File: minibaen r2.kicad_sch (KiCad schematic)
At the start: 134 parts, among them SW1 SW_Push, SW2 RotaryEncoder_Switch, U1 ATmega32U2-A, U2 PRTR5V0U2X, Y1 Crystal_GND24_Small

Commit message: stagger
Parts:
- removed C1: 4.7n, Capacitor_SMD:C_0603_1608Metric, symbol Device:C_Small
- removed C2, C4: 22pF, Capacitor_SMD:C_0603_1608Metric, symbol Device:C_Small
- removed C3: 1uF, Capacitor_SMD:C_0603_1608Metric, symbol Device:C_Small
- removed C5, C6: 0.1uF, Capacitor_SMD:C_0603_1608Metric, symbol Device:C_Small
- removed C7: 10uF, Capacitor_SMD:C_0603_1608Metric, symbol Device:C_Small
- removed D46, D47, D48, D49, D50, D51, D52: D_Small, Diode_SMD:D_SOD-123, symbol Device:D_Small
- removed F1: 500mA, Fuse:Fuse_1206_3216Metric, symbol Device:Polyfuse_Small
- removed MX1, MX10, MX11, MX12, MX13, MX14, MX15, MX16, MX17, MX18, MX19, MX2, MX20, MX21, MX22, MX23, MX24, MX25, MX26, MX27, MX28, MX29, MX3, MX30, MX31, MX32, MX33, MX34, MX35, MX36, MX37, MX38, MX39, MX4, MX40, MX41, MX42, MX43, MX44, MX45, MX46, MX47, MX48, MX49, MX5, MX50, MX51, MX52, MX6, MX7, MX8, MX9: MX-NoLED, MX_Only:MXOnly-1U-NoLED, symbol keybage:MX-NoLED
- removed MX53, MX57: MX-NoLED, MX_Only:MXOnly-2U-ReversedStabilizers-NoLED, symbol keybage:MX-NoLED
- removed MX54, MX56, MX58: MX-NoLED, MX_Only:MXOnly-3U-ReversedStabilizers-NoLED, symbol keybage:MX-NoLED
- removed MX55: MX-NoLED, MX_Only:MXOnly-7U-ReversedStabilizers-NoLED, symbol keybage:MX-NoLED
- removed R1: 10k, Resistor_SMD:R_0603_1608Metric, symbol Device:R_Small
- removed R2: 22, Resistor_SMD:R_0603_1608Metric, symbol Device:R_Small
- removed R5, R6: 5k1, Resistor_SMD:R_0603_1608Metric, symbol Device:R_Small
- removed R7: 1M, Resistor_SMD:R_0603_1608Metric, symbol Device:R_Small
- removed SW1: SW_Push, Connector_PinHeader_2.54mm:PinHeader_1x02_P2.54mm_Vertical, symbol Switch:SW_Push
- removed SW2: RotaryEncoder_Switch, keebio:RotaryEncoder_EC11-no-legs, symbol Device:RotaryEncoder_Switch
- removed U1: ATmega32U2-A, Package_QFP:TQFP-32_7x7mm_P0.8mm, symbol MCU_Microchip_ATmega:ATmega32U2-A
- removed U2: PRTR5V0U2X, Package_TO_SOT_SMD:SOT-143, symbol keebio:PRTR5V0U2X
- removed USB1: HRO-TYPE-C-31-M-12, Type-C:HRO-TYPE-C-31-M-12, symbol Type-C:HRO-TYPE-C-31-M-12
- removed Y1: Crystal_GND24_Small, Crystal:Crystal_SMD_3225-4Pin_3.2x2.5mm, symbol Device:Crystal_GND24_Small
- added C10, C11, C8, C9: 100nF, Capacitor_SMD:C_0402_1005Metric, symbol Device:C_Small
- added C12: 10nF, Capacitor_SMD:C_0402_1005Metric, symbol Device:C_Small
- added C13, C14, C19: 4.7uF, Capacitor_SMD:C_0402_1005Metric, symbol Device:C_Small
- added C15, C16, C17, C18: 1uF, Capacitor_SMD:C_0402_1005Metric, symbol Device:C_Small
- added F1: 500mA, Fuse:Fuse_0603_1608Metric, symbol Device:Fuse_Small
- added J1: USB_C_Receptacle_USB2.0, Connector_USB:USB_C_Receptacle_HRO_TYPE-C-31-M-12, symbol Connector:USB_C_Receptacle_USB2.0
- added Q1: 2N7002, Package_TO_SOT_SMD:SOT-23, symbol Transistor_FET:2N7002
- added R10, R11: 10k, Resistor_SMD:R_0402_1005Metric, symbol Device:R_Small
- added R12: 100k, Resistor_SMD:R_0402_1005Metric, symbol Device:R_Small
- added S1: MX_stab, marbastlib-mx:STAB_MX_2.75u, symbol marbastlib-mx:MX_stab
- added S2: MX_stab, marbastlib-mx:STAB_MX_3u, symbol marbastlib-mx:MX_stab
- added S3: MX_stab, marbastlib-mx:STAB_MX_2u, symbol marbastlib-mx:MX_stab
- added SW1, SW10, SW11, SW12, SW13, SW15, SW16, SW17, SW18, SW19, SW2, SW20, SW21, SW22, SW23, SW24, SW27, SW28, SW29, SW3, SW30, SW31, SW32, SW33, SW34, SW35, SW36, SW39, SW4, SW41, SW42, SW44, SW5, SW6, SW7, SW8, SW9: MX_SW_solder, marbastlib-mx:SW_MX_1u, symbol marbastlib-mx:MX_SW_solder
- added SW14, SW37, SW38, SW40, SW43, SW45: MX_SW_solder, marbastlib-mx:SW_MX_1.25u, symbol marbastlib-mx:MX_SW_solder
- added SW25, SW26: MX_SW_solder, marbastlib-mx:SW_MX_1.75u, symbol marbastlib-mx:MX_SW_solder
- added SW46: SW_Push, Button_Switch_SMD:SW_SPST_TL3342, symbol Switch:SW_Push
- added U3: SRV05-4, marbastlib-various:SOT-23-6-routable, symbol Power_Protection:SRV05-4
- added U4: XC6206PxxxMR, Package_TO_SOT_SMD:SOT-23, symbol Regulator_Linear:XC6206PxxxMR
- added U5: STM32F072C8Tx, Package_QFP:LQFP-48_7x7mm_P0.5mm, symbol MCU_ST_STM32F0:STM32F072C8Tx
- R3: value 22 -> 5k1; footprint Resistor_SMD:R_0603_1608Metric -> Resistor_SMD:R_0402_1005Metric
- R4: value 10k -> 5k1; footprint Resistor_SMD:R_0603_1608Metric -> Resistor_SMD:R_0402_1005Metric
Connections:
- net DP- is gone; now on net GND: R3.1
- net +5V: now also C16.2, F1.2, U4.3 (VI)
- net D+: now also J1.A6 (D+), J1.B6 (D+), U3.3 (IO2), U5.33 (PA12)
- net D-: now also J1.A7 (D-), J1.B7 (D-), U3.4 (IO3), U5.32 (PA11); no longer R3.2
- net GND: now also C10.2, C11.2, C12.2, C13.2, C14.2, C15.2, C16.1, C17.1, C18.2, C8.2, C9.2, J1.A1 (GND), J1.A12 (GND), J1.B1 (GND), J1.B12 (GND), J1.S1 (SHIELD), Q1.2 (S), R11.2, R12.2, U3.2 (VN), U4.1 (GND), U5.23 (VSS), U5.35 (VSS), U5.47 (VSS), U5.8 (VSSA)
- net col0: now also SW1.1, SW14.1, SW26.1, SW38.1, U5.18 (PB0)
- net col1: now also SW15.1, SW2.1, SW39.1, U5.17 (PA7)
- net col10: now also SW11.1, SW24.1, SW35.1, SW43.1, U5.25 (PB12)
- net col11: now also SW12.2, SW36.1, SW44.1, U5.37 (PA14)
- net col12: now also SW13.1, SW25.1, SW37.1, SW45.1, U5.46 (PB9)
- net col2: now also SW16.1, SW27.1, SW3.1, U5.16 (PA6)
- net col3: now also SW17.1, SW28.1, SW4.1, SW40.1, U5.15 (PA5)
- net col4: now also SW18.1, SW29.1, SW5.1, U5.31 (PA10)
- net col5: now also SW19.1, SW30.1, SW41.1, SW6.1, U5.30 (PA9)
- net col6: now also SW20.1, SW31.1, SW7.1, U5.29 (PA8)
- net col7: now also SW21.1, SW32.1, SW8.1, U5.28 (PB15)
- net col8: now also SW22.1, SW33.1, SW42.1, SW9.1, U5.27 (PB14)
- net col9: now also SW10.1, SW23.1, SW34.1, U5.26 (PB13)
- net row0: now also U5.38 (PA15)
- net row1: now also U5.41 (PB5); no longer D26.1 (K)
- net row2: now also D26.1 (K), U5.40 (PB4); no longer D38.1 (K), D39.1 (K)
- net row3: now also D38.1 (K), D39.1 (K), U5.39 (PB3)
- net at R4.2: now also J1.B5 (CC2)
- net at D43.2 (A): now also SW43.2
- net at D3.2 (A): now also SW3.2
- net at D39.2 (A): now also SW39.2
- net at D8.2 (A): now also SW8.2
- net at D25.2 (A): now also SW25.2
- net at D21.2 (A): now also SW21.2
- net at D2.2 (A): now also SW2.2
- net at D12.2 (A): now also SW12.1
- net at D33.2 (A): now also SW33.2
- net at D28.2 (A): now also SW28.2
- net at D19.2 (A): now also SW19.2
- net at D45.2 (A): now also SW45.2
- net at D38.2 (A): now also SW38.2
- net at D35.2 (A): now also SW35.2
- net at D22.2 (A): now also SW22.2
- net at D11.2 (A): now also SW11.2
- net at D1.2 (A): now also SW1.2
- net at D42.2 (A): now also SW42.2
- net at D13.2 (A): now also SW13.2
- net at D34.2 (A): now also SW34.2
- net at D7.2 (A): now also SW7.2
- net at D23.2 (A): now also SW23.2
- net at D41.2 (A): now also SW41.2
- net at D14.2 (A): now also SW14.2
- net at D40.2 (A): now also SW40.2
- net at D44.2 (A): now also SW44.2
- net at D24.2 (A): now also SW24.2
- net at D4.2 (A): now also SW4.2
- net at D15.2 (A): now also SW15.2
- net at D10.2 (A): now also SW10.2
- net at D9.2 (A): now also SW9.2
- net at D20.2 (A): now also SW20.2
- net at D16.2 (A): now also SW16.2
- net at D36.2 (A): now also SW36.2
- net at D6.2 (A): now also SW6.2
- net at D18.2 (A): now also SW18.2
- net at D31.2 (A): now also SW31.2
- net at D17.2 (A): now also SW17.2
- net at D30.2 (A): now also SW30.2
- net at D27.2 (A): now also SW27.2
- net at D5.2 (A): now also SW5.2
- net at D37.2 (A): now also SW37.2
- net at D32.2 (A): now also SW32.2
- net at D26.2 (A): now also SW26.2
- net at D29.2 (A): now also SW29.2
- new net: C19.2, Q1.1 (G), R12.1
- new net: J1.A5 (CC1), R3.2
- new net +3V3: C10.1, C11.1, C12.1, C13.1, C14.1, C15.1, C17.2, C8.1, C9.1, R10.1, SW46.2, U4.2 (VO), U5.1 (VBAT), U5.24 (VDD), U5.36 (VDDIO2), U5.48 (VDD), U5.9 (VDDA)
- new net BOOT0: C19.1, R11.1, SW46.1, U5.44 (BOOT0)
- new net NRST: C18.1, Q1.3 (D), R10.2, U5.7 (NRST)
- new net VBUS: F1.1, J1.A4 (VBUS), J1.A9 (VBUS), J1.B4 (VBUS), J1.B9 (VBUS), U3.5 (VP)
- no-connect marks 2 -> 4
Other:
- note added: "Decoupling Capacitors"
- note added: "ESD Protection"
- note added: "MCU"
- note added: "Reset Switch"
- note added: "USB"
- note added: "Voltage Regulator"
- moved on the sheet: H1, H2, H3

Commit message: uhhhhh
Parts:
- added H4, H5: MountingHole, MountingHole:MountingHole_2.2mm_M2_DIN965_Pad, symbol Mechanical:MountingHole
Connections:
- net col4: now also U5.14 (PA4); no longer U5.31 (PA10)
- net col5: now also U5.13 (PA3); no longer U5.30 (PA9)
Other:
- moved on the sheet: H1, H2, H3
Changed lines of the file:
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@@
     (stroke (width 0) (type default))
   )
+  (polyline (pts (xy 156.972 57.658) (xy 156.972 11.938))
+    (stroke (width 0) (type default))
+  )
   (wire (pts (xy 52.324 146.05) (xy 52.324 157.48))
     (stroke (width 0) (type default))
@@
     (stroke (width 0) (type default))
   )
+  (polyline (pts (xy 201.422 113.538) (xy 201.422 57.658))
+    (stroke (width 0) (type default))
+  )
   (wire (pts (xy 101.092 18.288) (xy 106.172 18.288))
     (stroke (width 0) (type default))
@@
     )
   )
-  (global_label "col4" (shape input) (at 57.912 80.518 0) (fields_autoplaced)
+  (global_label "col4" (shape input) (at 57.912 65.278 0) (fields_autoplaced)
     (effects (font (size 1.27 1.27)) (justify left))
-    (property "Intersheetrefs" "${INTERSHEET_REFS}" (at 65.0252 80.518 0)
+    (property "Intersheetrefs" "${INTERSHEET_REFS}" (at 65.0252 65.278 0)
       (effects (font (size 1.27 1.27)) (justify left) hide)
     )
@@
     )
   )
-  (global_label "col5" (shape input) (at 57.912 77.978 0) (fields_autoplaced)
+  (global_label "col5" (shape input) (at 57.912 62.738 0) (fields_autoplaced)
     (effects (font (size 1.27 1.27)) (justify left))
-    (property "Intersheetrefs" "${INTERSHEET_REFS}" (at 65.0252 77.978 0)
+    (property "Intersheetrefs" "${INTERSHEET_REFS}" (at 65.0252 62.738 0)
       (effects (font (size 1.27 1.27)) (justify left) hide)
     )
@@
     )
   )
-  (symbol (lib_id "Mechanical:MountingHole") (at 226.187 16.764 0) (unit 1)
+  (symbol (lib_id "Mechanical:MountingHole") (at 70.866 32.512 0) (unit 1)
     (in_bom yes) (on_board yes) (dnp no) (fields_autoplaced)
-    (property "Reference" "H1" (at 229.997 16.1289 0)
+    (property "Reference" "H1" (at 74.676 31.8769 0)
       (effects (font (size 1.27 1.27)) (justify left))
     )
-    (property "Value" "MountingHole" (at 229.997 18.6689 0)
+    (property "Value" "MountingHole" (at 74.676 34.4169 0)
       (effects (font (size 1.27 1.27)) (justify left))
     )
-    (property "Footprint" "MountingHole:MountingHole_2.2mm_M2_DIN965_Pad" (at 226.187 16.764 0)
+    (property "Footprint" "MountingHole:MountingHole_2.2mm_M2_DIN965_Pad" (at 70.866 32.512 0)
       (effects (font (size 1.27 1.27)) hide)
     )
-    (property "Datasheet" "~" (at 226.187 16.764 0)
+    (property "Datasheet" "~" (at 70.866 32.512 0)
       (effects (font (size 1.27 1.27)) hide)
     )
@@
     )
   )
+  (symbol (lib_id "Mechanical:MountingHole") (at 90.424 37.846 0) (unit 1)
+    (in_bom yes) (on_board yes) (dnp no) (fields_autoplaced)
+    (property "Reference" "H5" (at 94.234 37.2109 0)
+      (effects (font (size 1.27 1.27)) (justify left))
+    )
+    (property "Value" "MountingHole" (at 94.234 39.7509 0)
+      (effects (font (size 1.27 1.27)) (justify left))
+    )
+    (property "Footprint" "MountingHole:MountingHole_2.2mm_M2_DIN965_Pad" (at 90.424 37.846 0)
+      (effects (font (size 1.27 1.27)) hide)
+    )
+    (property "Datasheet" "~" (at 90.424 37.846 0)
+      (effects (font (size 1.27 1.27)) hide)
+    )
+    (instances
+      (project "minibaen r2"
+        (path "/f373dbbd-24c9-4966-b78d-facf605ea15a"
+          (reference "H5") (unit 1)
+        )
+      )
+    )
+  )
   (symbol (lib_id "power:GND") (at 41.402 98.298 0) (unit 1)
     (in_bom yes) (on_board yes) (dnp no) (fields_autoplaced)
@@
     )
   )
+  (symbol (lib_id "Mechanical:MountingHole") (at 90.424 32.766 0) (unit 1)
+    (in_bom yes) (on_board yes) (dnp no) (fields_autoplaced)
+    (property "Reference" "H4" (at 94.234 32.1309 0)
+      (effects (font (size 1.27 1.27)) (justify left))
+    )
+    (property "Value" "MountingHole" (at 94.234 34.6709 0)
+      (effects (font (size 1.27 1.27)) (justify left))
+    )
+    (property "Footprint" "MountingHole:MountingHole_2.2mm_M2_DIN965_Pad" (at 90.424 32.766 0)
+      (effects (font (size 1.27 1.27)) hide)
+    )
+    (property "Datasheet" "~" (at 90.424 32.766 0)
+      (effects (font (size 1.27 1.27)) hide)
+    )
+    (instances
+      (project "minibaen r2"
+        (path "/f373dbbd-24c9-4966-b78d-facf605ea15a"
+          (reference "H4") (unit 1)
+        )
+      )
+    )
+  )
   (symbol (lib_id "Device:D_Small") (at 57.404 153.67 90) (unit 1)
     (in_bom yes) (on_board yes) (dnp no)
@@
     )
   )
-  (symbol (lib_id "Mechanical:MountingHole") (at 232.537 16.764 0) (unit 1)
+  (symbol (lib_id "Mechanical:MountingHole") (at 70.866 37.592 0) (unit 1)
     (in_bom yes) (on_board yes) (dnp no) (fields_autoplaced)
-    (property "Reference" "H2" (at 236.347 16.1289 0)
+    (property "Reference" "H2" (at 74.676 36.9569 0)
       (effects (font (size 1.27 1.27)) (justify left))
     )
-    (property "Value" "MountingHole" (at 236.347 18.6689 0)
+    (property "Value" "MountingHole" (at 74.676 39.4969 0)
       (effects (font (size 1.27 1.27)) (justify left))
     )
-    (property "Footprint" "MountingHole:MountingHole_2.2mm_M2_DIN965_Pad" (at 232.537 16.764 0)
+    (property "Footprint" "MountingHole:MountingHole_2.2mm_M2_DIN965_Pad" (at 70.866 37.592 0)
       (effects (font (size 1.27 1.27)) hide)
     )
-    (property "Datasheet" "~" (at 232.537 16.764 0)
+    (property "Datasheet" "~" (at 70.866 37.592 0)
       (effects (font (size 1.27 1.27)) hide)
     )
@@
     )
   )
-  (symbol (lib_id "Mechanical:MountingHole") (at 242.062 16.764 0) (unit 1)
+  (symbol (lib_id "Mechanical:MountingHole") (at 70.866 42.418 0) (unit 1)
     (in_bom yes) (on_board yes) (dnp no) (fields_autoplaced)
-    (property "Reference" "H3" (at 245.237 16.1289 0)
+    (property "Reference" "H3" (at 74.041 41.7829 0)
       (effects (font (size 1.27 1.27)) (justify left))
     )
-    (property "Value" "MountingHole" (at 245.237 18.6689 0)
+    (property "Value" "MountingHole" (at 74.041 44.3229 0)
       (effects (font (size 1.27 1.27)) (justify left))
     )
-    (property "Footprint" "MountingHole:MountingHole_2.2mm_M2_DIN965_Pad" (at 242.062 16.764 0)
+    (property "Footprint" "MountingHole:MountingHole_2.2mm_M2_DIN965_Pad" (at 70.866 42.418 0)
       (effects (font (size 1.27 1.27)) hide)
     )
-    (property "Datasheet" "~" (at 242.062 16.764 0)
+    (property "Datasheet" "~" (at 70.866 42.418 0)
       (effects (font (size 1.27 1.27)) hide)
     )

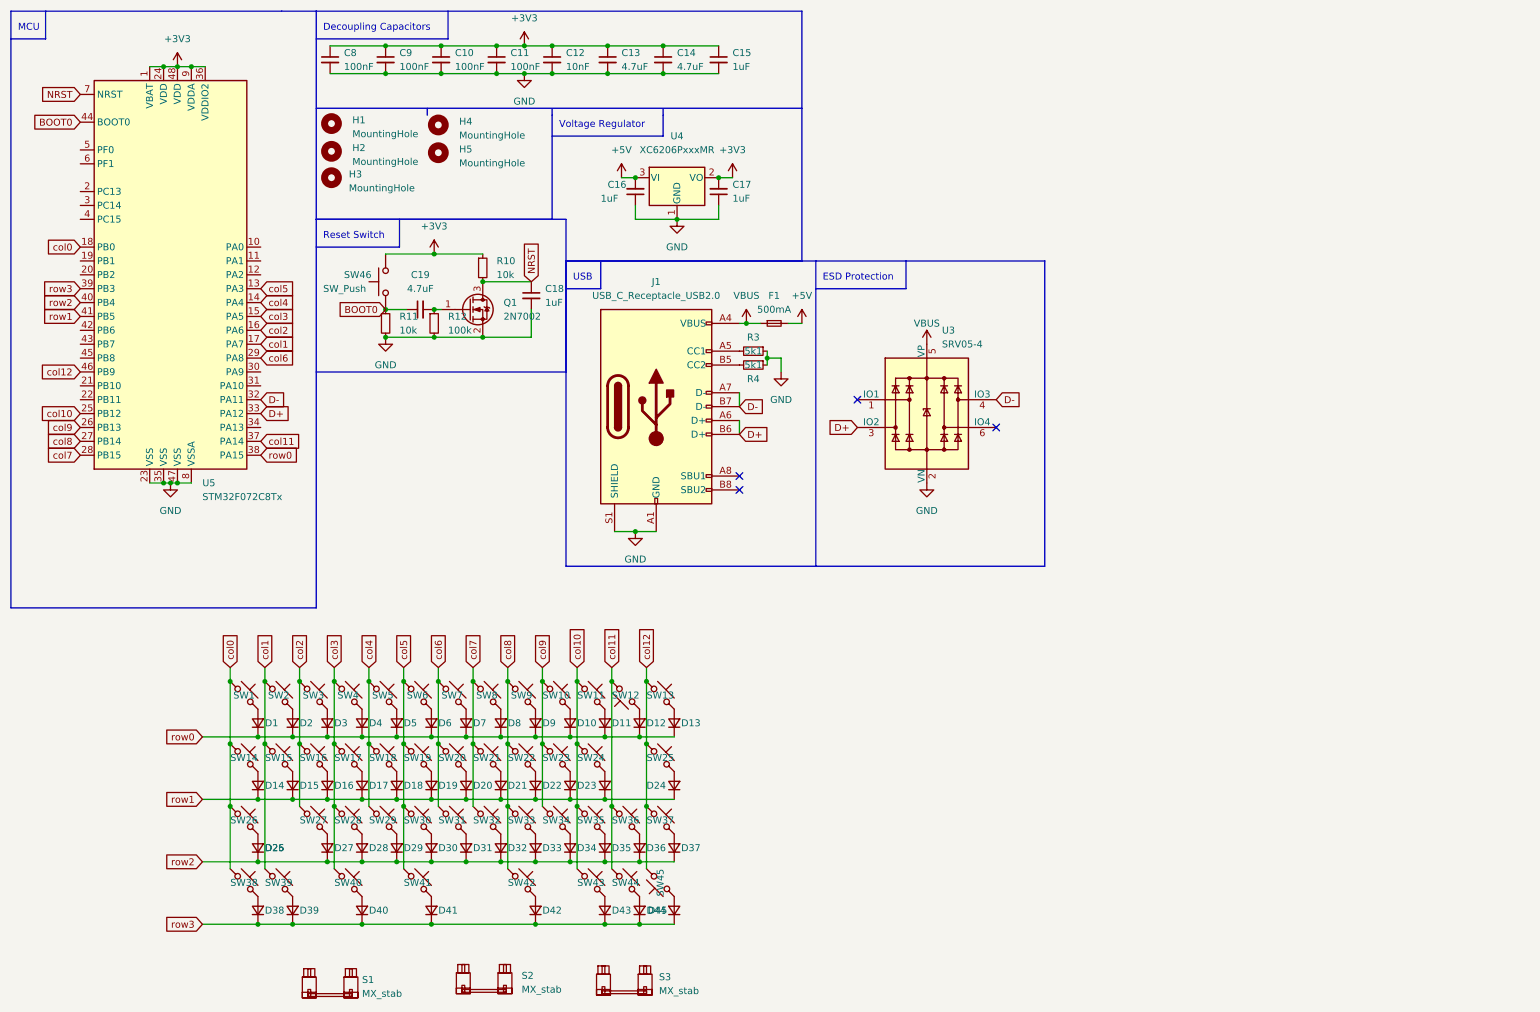
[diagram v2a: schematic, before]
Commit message: add jlcpcb plugin with complete bom, redo bottom row layout
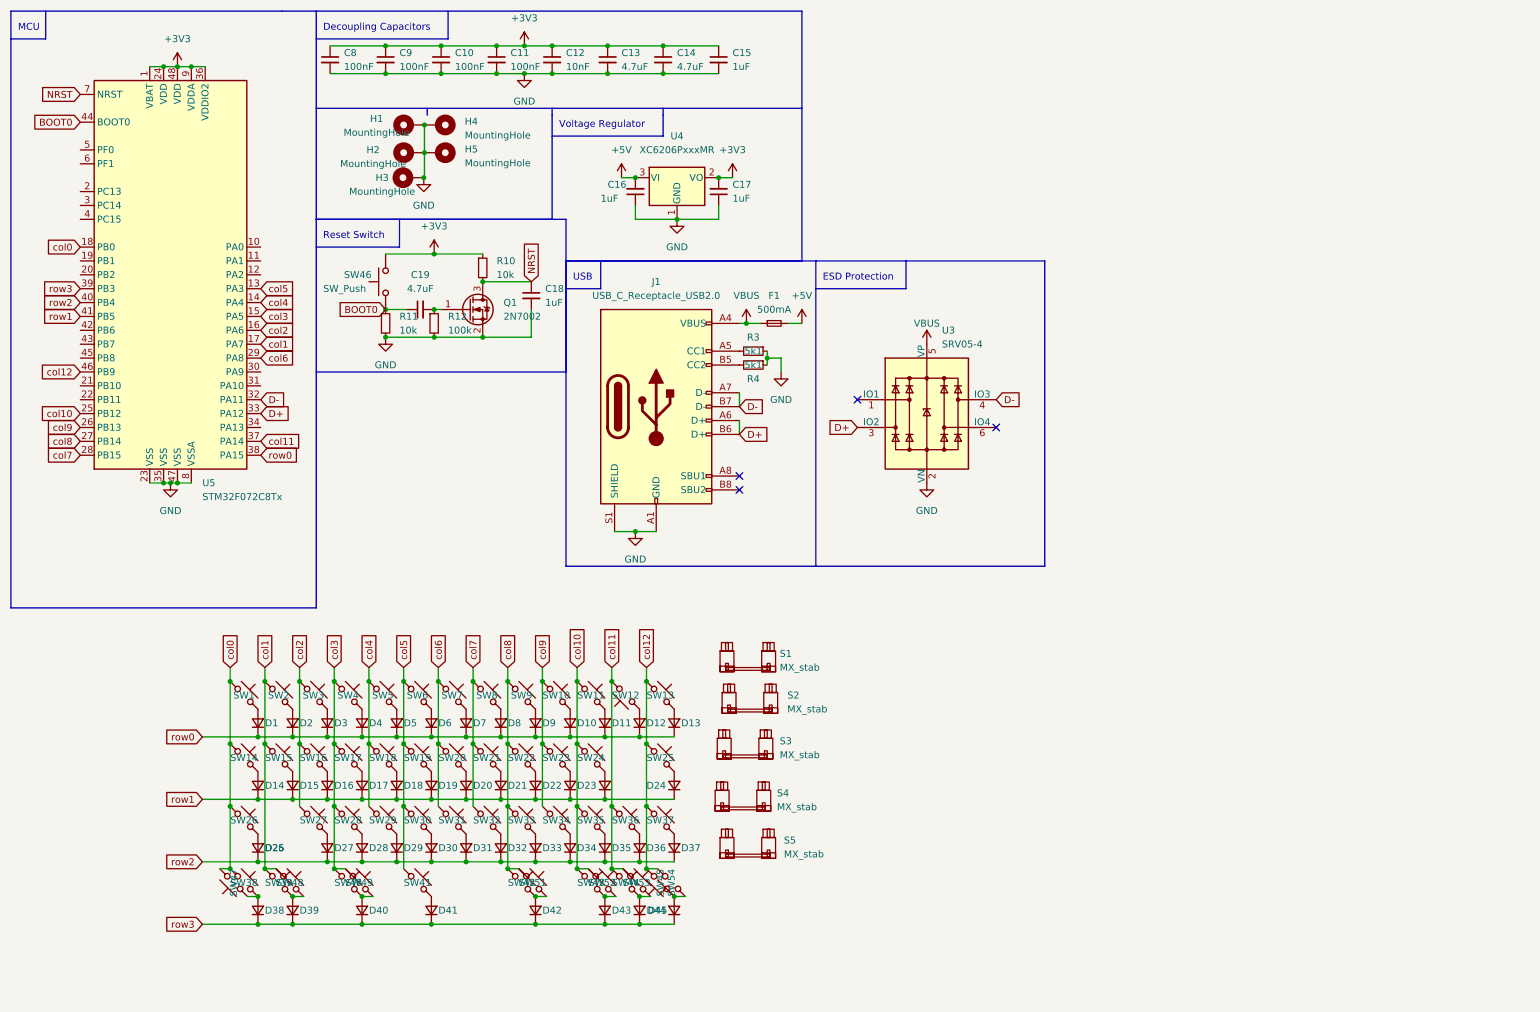
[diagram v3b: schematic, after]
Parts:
- added S4: MX_stab, marbastlib-mx:STAB_MX_2.75u, symbol marbastlib-mx:MX_stab
- added S5: MX_stab, marbastlib-mx:STAB_MX_2u, symbol marbastlib-mx:MX_stab
- added SW47, SW49, SW52, SW54: MX_SW_solder, marbastlib-mx:SW_MX_1.5u, symbol marbastlib-mx:MX_SW_solder
- added SW48, SW51, SW53: MX_SW_solder, marbastlib-mx:SW_MX_1u, symbol marbastlib-mx:MX_SW_solder
- H1, H2, H3, H4, H5: symbol Mechanical:MountingHole -> Mechanical:MountingHole_Pad
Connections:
- net GND: now also H1.1, H2.1, H3.1, H4.1, H5.1
- net col0: now also SW47.1
- net col1: now also SW48.1
- net col10: now also SW52.1
- net col11: now also SW53.1
- net col12: now also SW54.1
- net col3: now also SW49.1
- net col8: now also SW51.1
- net at D39.2 (A), SW39.2: now also SW48.2
- net at D45.2 (A), SW45.2: now also SW54.2
- net at D42.2 (A), SW42.2: now also SW51.2
- net at D44.2 (A), SW44.2: now also SW53.2
- net at D38.2 (A), SW38.2: now also SW47.2
- net at D40.2 (A), SW40.2: now also SW49.2
- net at D43.2 (A), SW43.2: now also SW52.2
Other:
- moved on the sheet: S1, S2, S3
